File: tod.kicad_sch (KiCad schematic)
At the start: 65 parts, among them J1 Conn_01x04, J2 Conn_01x03, J3 Conn_01x04, J4 Conn_01x03, Q1 BC856B, Q2 BC817, Q3 BC856B, Q4 BC817, Q5 BC856, Q6 BC817, Q7 BC856, Q8 BC817, U1 PC817, U2 PC817, U3 PC817, U4 PC817

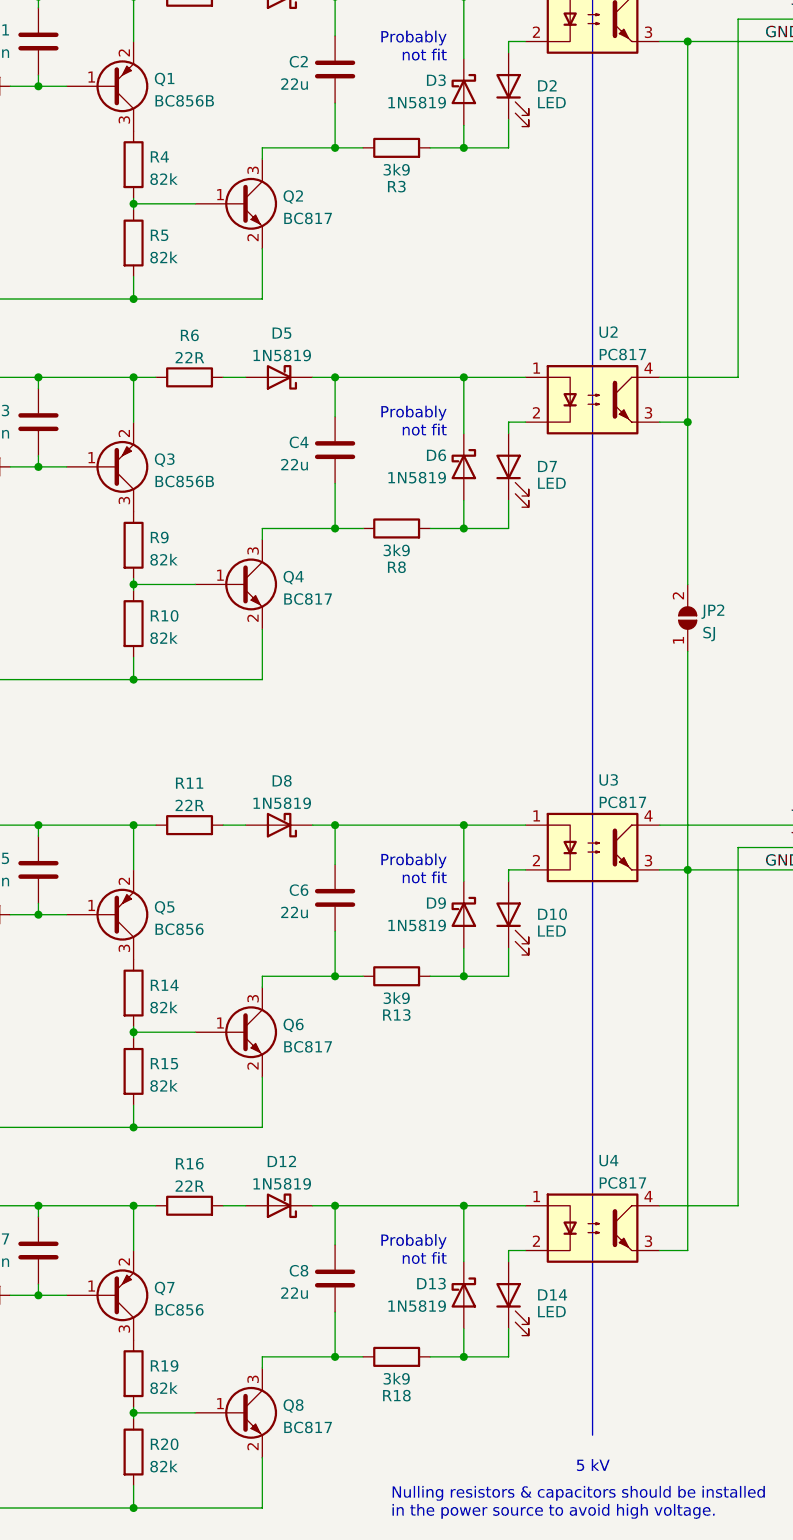
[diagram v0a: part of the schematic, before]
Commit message: Use 2k resistors instead of 3k9.
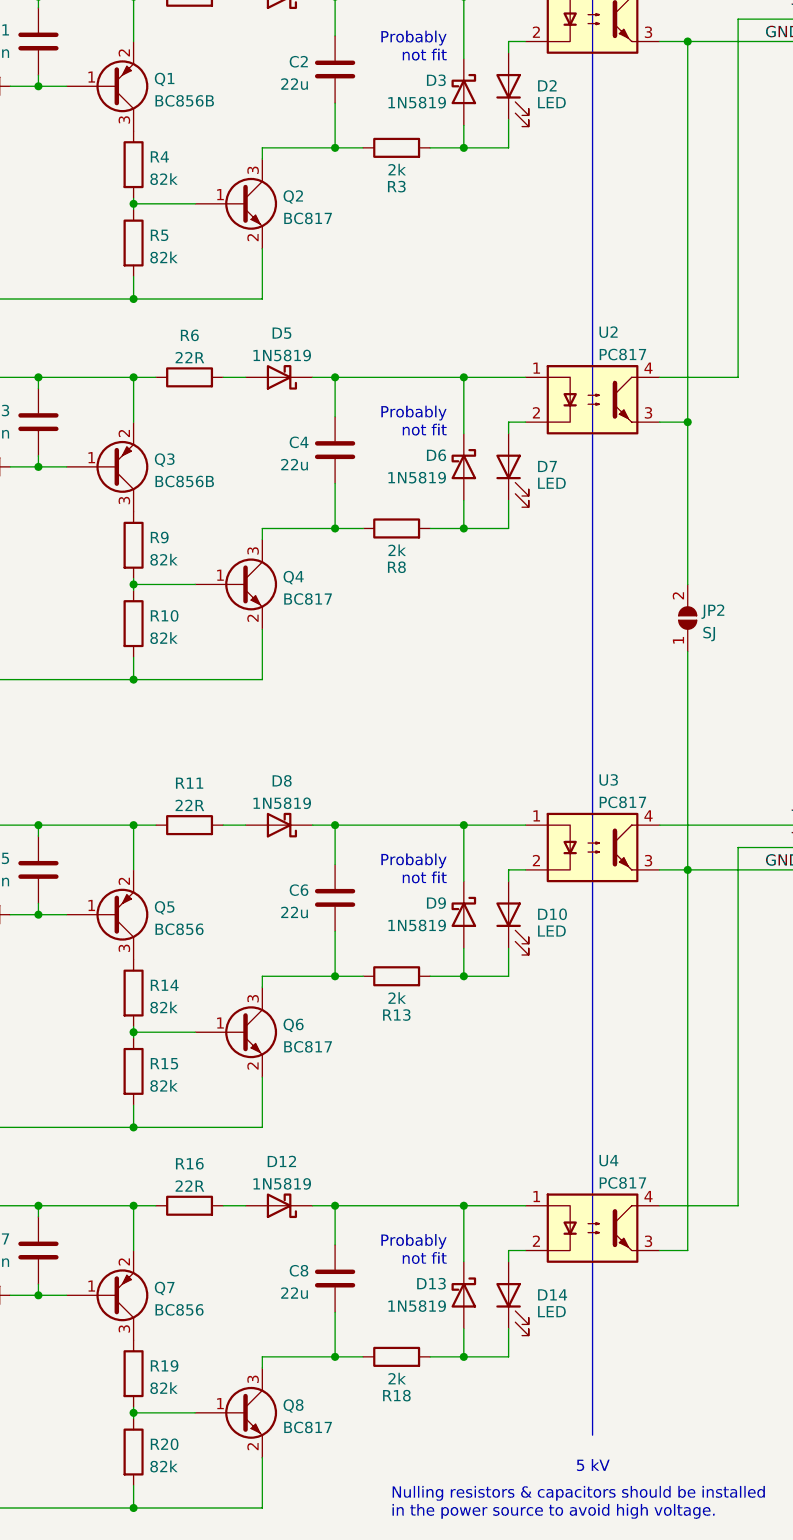
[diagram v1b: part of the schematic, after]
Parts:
- R13, R18, R3, R8: value 3k9 -> 2k; LCSC C17614 -> C17604
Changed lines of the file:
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@@
   (symbol (lib_id "Graphic:Logo_Open_Hardware_Small") (at 275.082 157.988 0) (unit 1)
     (in_bom yes) (on_board yes) (fields_autoplaced)
-    (property "Reference" "#LOGO?" (id 0) (at 275.082 151.003 0)
+    (property "Reference" "#LOGO1" (id 0) (at 275.082 151.003 0)
       (effects (font (size 1.27 1.27)) hide)
     )
@@
     (in_bom yes) (on_board yes)
     (property "Reference" "R3" (id 0) (at 123.825 43.18 90))
-    (property "Value" "3k9" (id 1) (at 123.825 41.275 90))
+    (property "Value" "2k" (id 1) (at 123.825 41.275 90))
     (property "Footprint" "Resistor_SMD:R_0805_2012Metric_Pad1.20x1.40mm_HandSolder" (id 2) (at 123.825 40.513 90)
       (effects (font (size 1.27 1.27)) hide)
@@
       (effects (font (size 1.27 1.27)) hide)
     )
-    (property "LCSC" "C17614" (id 4) (at 123.825 38.735 0)
+    (property "LCSC" "C17604" (id 4) (at 123.825 38.735 0)
       (effects (font (size 1.27 1.27)) hide)
     )
@@
     (in_bom yes) (on_board yes)
     (property "Reference" "R8" (id 0) (at 123.825 86.36 90))
-    (property "Value" "3k9" (id 1) (at 123.825 84.455 90))
+    (property "Value" "2k" (id 1) (at 123.825 84.455 90))
     (property "Footprint" "Resistor_SMD:R_0805_2012Metric_Pad1.20x1.40mm_HandSolder" (id 2) (at 123.825 83.693 90)
       (effects (font (size 1.27 1.27)) hide)
@@
       (effects (font (size 1.27 1.27)) hide)
     )
-    (property "LCSC" "C17614" (id 4) (at 123.825 81.915 0)
+    (property "LCSC" "C17604" (id 4) (at 123.825 81.915 0)
       (effects (font (size 1.27 1.27)) hide)
     )
@@
     (in_bom yes) (on_board yes)
     (property "Reference" "R18" (id 0) (at 123.825 180.34 90))
-    (property "Value" "3k9" (id 1) (at 123.825 178.435 90))
+    (property "Value" "2k" (id 1) (at 123.825 178.435 90))
     (property "Footprint" "Resistor_SMD:R_0805_2012Metric_Pad1.20x1.40mm_HandSolder" (id 2) (at 123.825 177.673 90)
       (effects (font (size 1.27 1.27)) hide)
@@
       (effects (font (size 1.27 1.27)) hide)
     )
-    (property "LCSC" "C17614" (id 4) (at 123.825 175.895 0)
+    (property "LCSC" "C17604" (id 4) (at 123.825 175.895 0)
       (effects (font (size 1.27 1.27)) hide)
     )
@@
     (in_bom yes) (on_board yes)
     (property "Reference" "R13" (id 0) (at 123.825 137.16 90))
-    (property "Value" "3k9" (id 1) (at 123.825 135.255 90))
+    (property "Value" "2k" (id 1) (at 123.825 135.255 90))
     (property "Footprint" "Resistor_SMD:R_0805_2012Metric_Pad1.20x1.40mm_HandSolder" (id 2) (at 123.825 134.493 90)
       (effects (font (size 1.27 1.27)) hide)
@@
       (effects (font (size 1.27 1.27)) hide)
     )
-    (property "LCSC" "C17614" (id 4) (at 123.825 132.715 0)
+    (property "LCSC" "C17604" (id 4) (at 123.825 132.715 0)
       (effects (font (size 1.27 1.27)) hide)
     )
@@
   (symbol_instances
     (path "/361cc21e-47c7-4d2d-b684-c4ecf46e1791"
-      (reference "#LOGO?") (unit 1) (value "Logo_Open_Hardware_Small") (footprint "")
+      (reference "#LOGO1") (unit 1) (value "Logo_Open_Hardware_Small") (footprint "")
     )
     (path "/949e12d6-32f4-4bfa-9bdc-0a2dc68d9702"
@@
     )
     (path "/6482a8d5-54ad-47be-8272-081fe112eec4"
-      (reference "R3") (unit 1) (value "3k9") (footprint "Resistor_SMD:R_0805_2012Metric_Pad1.20x1.40mm_HandSolder")
+      (reference "R3") (unit 1) (value "2k") (footprint "Resistor_SMD:R_0805_2012Metric_Pad1.20x1.40mm_HandSolder")
     )
     (path "/78c42f87-2789-4e07-b18d-8f8b5409a989"
@@
     )
     (path "/ad5e9409-abbd-41d0-a4a7-824ec612606c"
-      (reference "R8") (unit 1) (value "3k9") (footprint "Resistor_SMD:R_0805_2012Metric_Pad1.20x1.40mm_HandSolder")
+      (reference "R8") (unit 1) (value "2k") (footprint "Resistor_SMD:R_0805_2012Metric_Pad1.20x1.40mm_HandSolder")
     )
     (path "/03771697-dfea-4597-9909-b3909b334a64"
@@
     )
     (path "/f08c1b46-15a3-4269-a58c-f504dad3ff5c"
-      (reference "R13") (unit 1) (value "3k9") (footprint "Resistor_SMD:R_0805_2012Metric_Pad1.20x1.40mm_HandSolder")
+      (reference "R13") (unit 1) (value "2k") (footprint "Resistor_SMD:R_0805_2012Metric_Pad1.20x1.40mm_HandSolder")
     )
     (path "/c7861c30-7054-427f-b1e2-1f003c1d4aa4"
@@
     )
     (path "/b4d0cd47-ee70-4cd4-921c-1bfdb9da9a6f"
-      (reference "R18") (unit 1) (value "3k9") (footprint "Resistor_SMD:R_0805_2012Metric_Pad1.20x1.40mm_HandSolder")
+      (reference "R18") (unit 1) (value "2k") (footprint "Resistor_SMD:R_0805_2012Metric_Pad1.20x1.40mm_HandSolder")
     )
     (path "/54f5c2ae-e7ec-4883-ab5a-237e9f7ba07b"

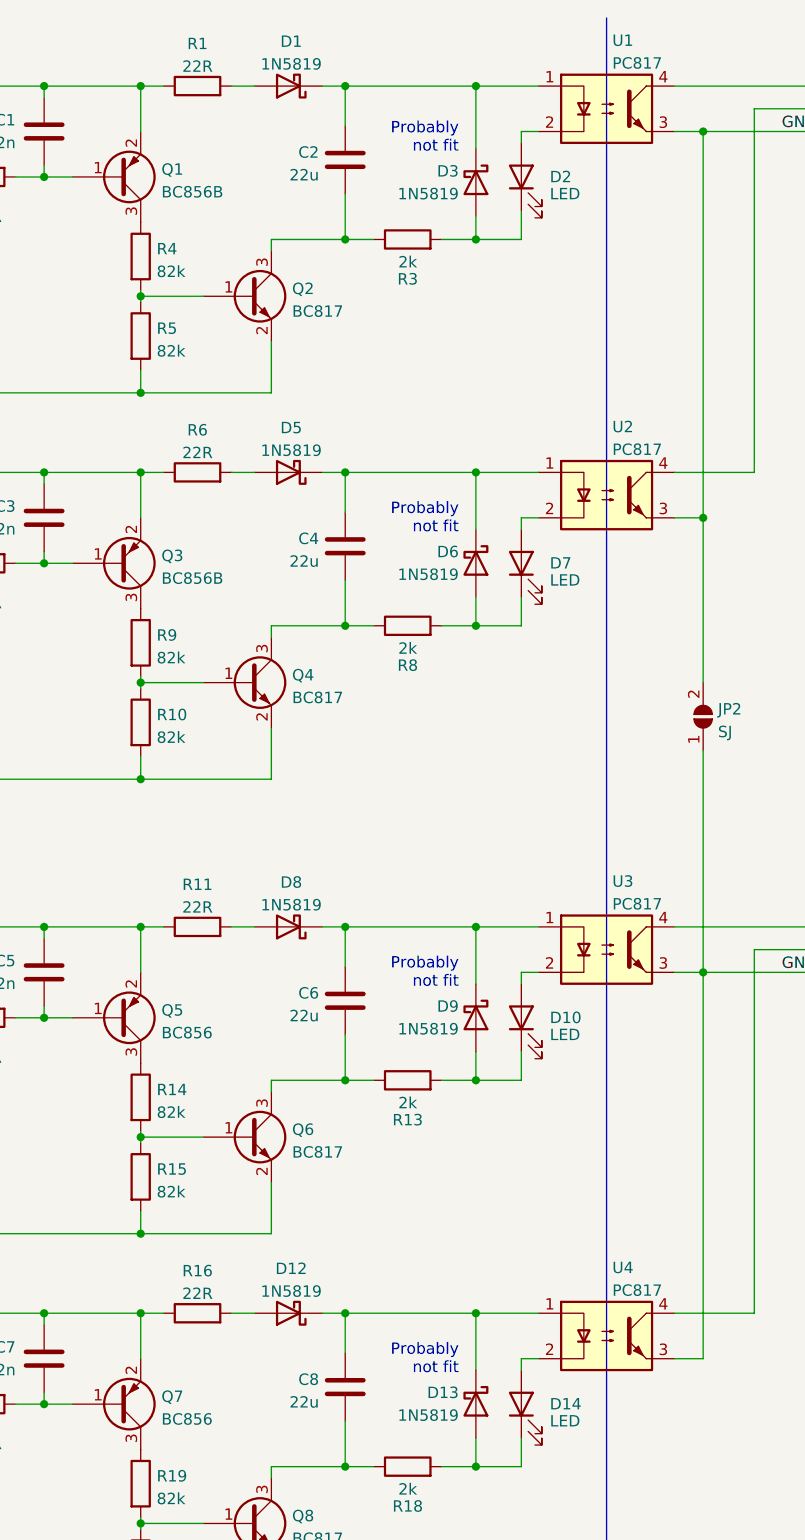
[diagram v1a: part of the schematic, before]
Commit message: Really do not fit unused diodes.
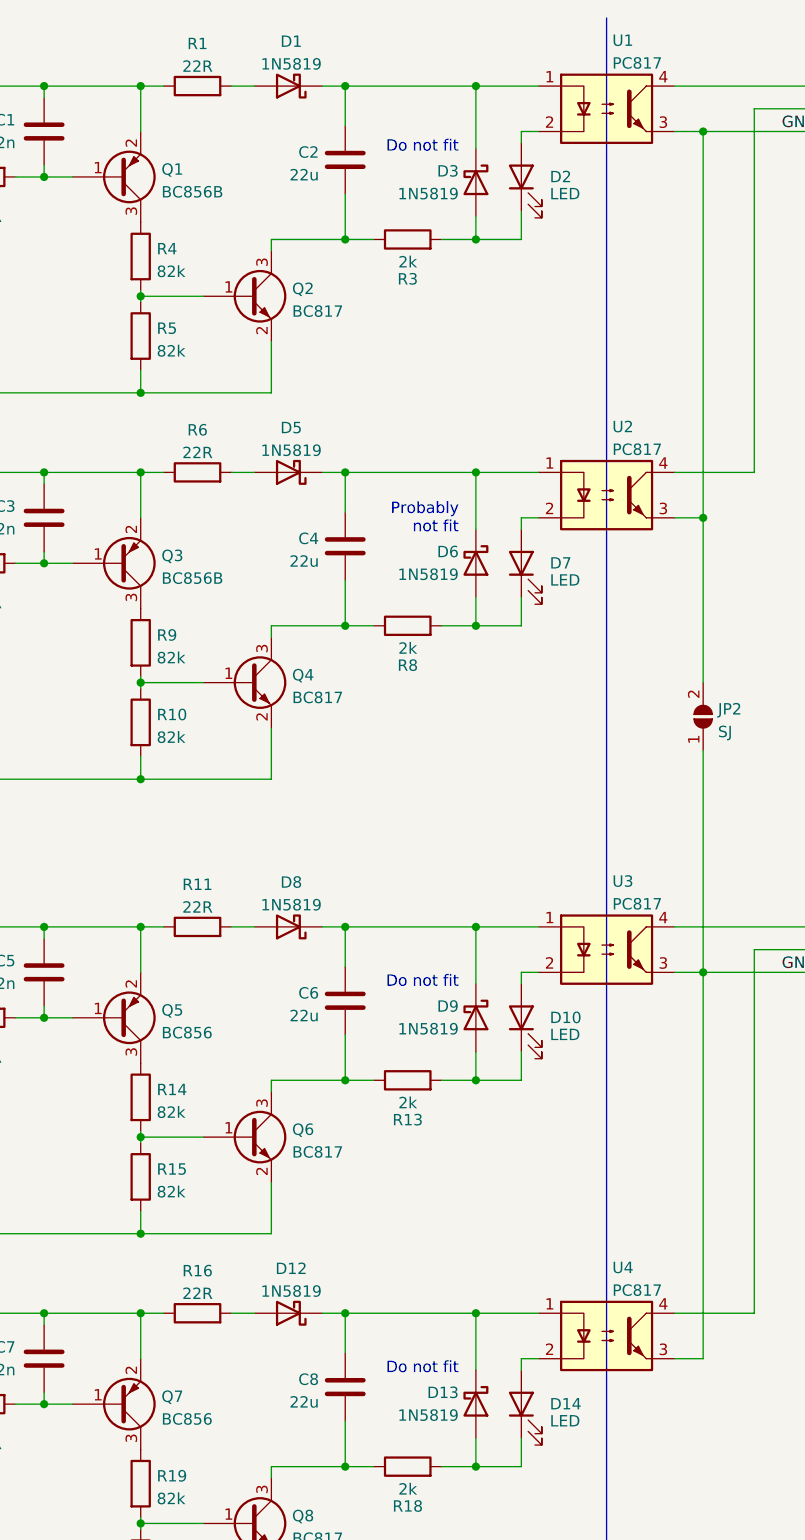
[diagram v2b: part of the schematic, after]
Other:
- note added: "Do not fit"
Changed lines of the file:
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@@
     (stroke (width 0) (type default) (color 0 0 0 0))
   )
-  (text "Probably\nnot fit" (at 129.54 165.735 180)
+  (text "Do not fit" (at 129.54 165.735 180)
     (effects (font (size 1.27 1.27)) (justify right bottom))
   )
@@
     (effects (font (size 1.27 1.27)) (justify left bottom))
   )
-  (text "Probably\nnot fit" (at 129.54 122.555 180)
+  (text "Do not fit" (at 129.54 122.555 180)
     (effects (font (size 1.27 1.27)) (justify right bottom))
   )
-  (text "Probably\nnot fit" (at 129.54 29.21 180)
+  (text "Do not fit" (at 129.54 29.21 180)
     (effects (font (size 1.27 1.27)) (justify right bottom))
   )
